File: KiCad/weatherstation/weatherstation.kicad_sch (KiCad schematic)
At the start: 5 parts, among them U1 ESP32_NODEMCU, U2 AM2302, U3 AM2302

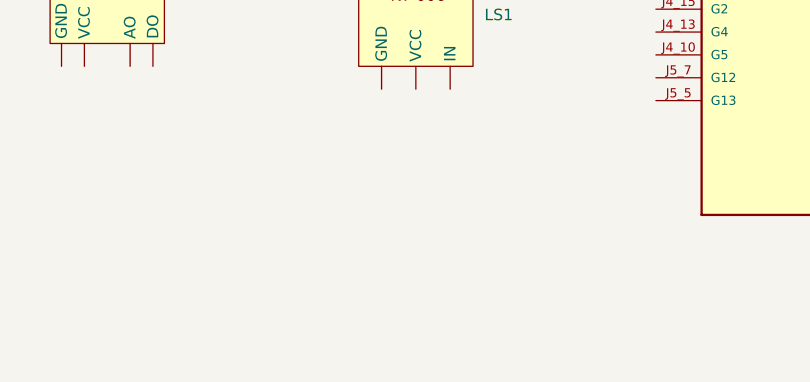
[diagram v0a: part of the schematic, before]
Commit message: Added BMS in Readme
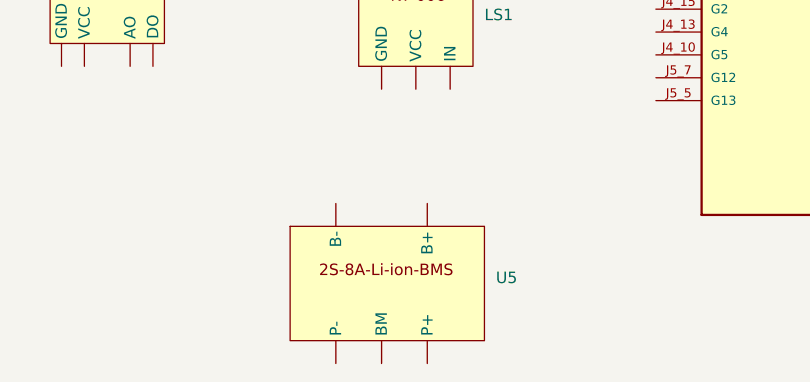
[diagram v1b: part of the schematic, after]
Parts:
- added U5: ~, symbol weatherstation:2S-8A-Li-ion-Lithium-18650-BMS{lt}
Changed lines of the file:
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@@
+	)
+	(symbol
+		(lib_id "weatherstation:2S-8A-Li-ion-Lithium-18650-BMS{lt}")
+		(at 86.36 113.03 0)
+		(unit 1)
+		(exclude_from_sim no)
+		(in_bom yes)
+		(on_board yes)
+		(dnp no)
+		(fields_autoplaced yes)
+		(property "Reference" "U5"
+			(at 99.06 112.3949 0)
+			(effects
+				(font
+					(size 1.27 1.27)
+				)
+				(justify left)
+			)
+		)
+		(property "Value" "~"
+			(at 99.06 114.3 0)
+			(effects
+				(font
+					(size 1.27 1.27)
+				)
+				(justify left)
+			)
+		)
+		(property "Footprint" ""
+			(at 86.36 113.03 0)
+			(effects
+				(font
+					(size 1.27 1.27)
+				)
+				(hide yes)
+			)
+		)
+		(property "Datasheet" ""
+			(at 86.36 113.03 0)
+			(effects
+				(font
+					(size 1.27 1.27)
+				)
+				(hide yes)
+			)
+		)
+		(property "Description" ""
+			(at 86.36 113.03 0)
+			(effects
+				(font
+					(size 1.27 1.27)
+				)
+				(hide yes)
+			)
+		)
+		(pin ""
+		)
+		(pin ""
+		)
+		(pin ""
+		)
+		(pin ""
+		)
+		(pin ""
+		)
+		(instances
+			(project ""
+				(path "/71de8abf-2b78-47ee-a11c-22c83be02bb1"
+					(reference "U5")
+					(unit 1)
+				)
+			)
+		)
 	)
 	(symbol

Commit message: dighdfiug
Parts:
- removed U1: ESP32_NODEMCU, ESP32_NODEMCU:MODULE_ESP32_NODEMCU, symbol weatherstation:ESP32_NODEMCU
- removed U2, U3: AM2302, Sensor:ASAIR_AM2302_P2.54mm_Vertical, symbol Sensor:AM2302
- removed U5: ~, symbol weatherstation:2S-8A-Li-ion-Lithium-18650-BMS{lt}
- added D1: LED, symbol Device:LED
- added Q1: NMOS, symbol Simulation_SPICE:NMOS
- added SW1: SW_SPST, symbol Switch:SW_SPST
- added U1: Pico, RPi_Pico:RPi_Pico_SMD_TH, symbol MCU_RaspberryPi_and_Boards:Pico
- added U2: ~, symbol weatherstation:bme280
- added U5: ~, symbol weatherstation:bh1750
- added U6: ~, symbol weatherstation:Step-up
- added U7: ~, symbol weatherstation:Battery-Charger-Module
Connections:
- net at U4. (VCC): now also Q1.1 (D), U2. (VIN), U5. (VCC)
- new net: U1.31 (GPIO26_ADC0), U4. (VCC)
- new net: U1.39 (VSYS), U2. (VIN), U4. (VCC), U5. (VCC), U6. (VOUT)
- new net: U1.1 (GPIO0), U2. (VIN), U5. (VCC)
- new net: Q1.3 (S), U1.13 (GND), U6. (VOUT)
- new net: U1.2 (GPIO1), U2. (VIN), U5. (VCC)
- new net: Q1.2 (G), U1.20 (GPIO15)
- new net: SW1.1 (A), U7. (OUT+)
- new net: U6. (VOUT), U7. (OUT+)
- new net: SW1.2 (B), U6. (VOUT)
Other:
- moved on the sheet: LS1, U4
